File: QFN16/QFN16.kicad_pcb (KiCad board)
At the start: 2 copper layers, 20.6 x 13 mm, 9 parts, among them J1 Conn_01x08, J2 Conn_02x08_Counter_Clockwise, J3 Conn_01x08, J4 Conn_02x08_Counter_Clockwise, J5 Conn_01x03

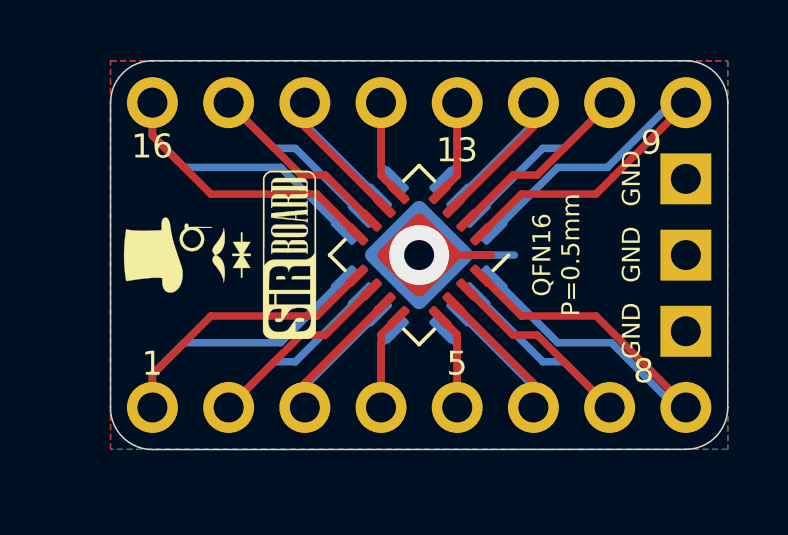
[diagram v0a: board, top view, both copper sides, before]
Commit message: Breakout Boards Revision 2
Renders updated, silkscreen text improved, blurry silkscreen items removed/resized.
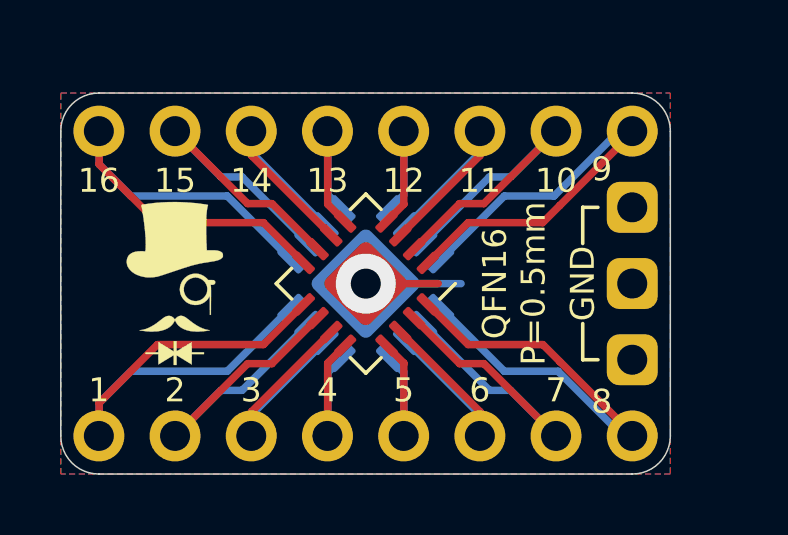
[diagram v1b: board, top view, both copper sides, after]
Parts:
- removed the G*** at (65.5, 41.0)
- removed the G*** at (62.4, 41.0)
- removed the G*** at (66.0, 41.0)
- added G***: LOGO, logo:logo54x76, B.Cu at (62.2, 41.9)
- G***: footprint logo:logo42x59 -> logo:logo54x76
- moved J3 2.02 mm to (77.5, 47.0)
- moved J1 2.02 mm to (77.5, 36.8)
- moved J5 2.02 mm to (77.5, 39.4)
- moved J2 2.02 mm to (68.6, 41.9)
- moved J4 2.02 mm to (68.6, 41.9)
- moved G*** 1.04 mm to (62.2, 41.9), turned to 0 degrees
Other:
- board size 20.6 x 13 mm -> 20.3 x 12.7 mm
- board text added: "10"
- board text added: "11"
- board text added: "12"
- board text added: "14"
- board text added: "15"
- board text added: "2"
- board text added: "3"
- board text added: "4"
- board text added: "6"
- board text added: "7"
